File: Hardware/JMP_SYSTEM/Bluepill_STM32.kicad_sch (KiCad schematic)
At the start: 2 parts, among them J1 BLUEPILL

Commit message: Schematics and PCB layout
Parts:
- removed J?: BLUEPILL, Package_DIP:DIP-40_W15.24mm_Socket_LongPads, symbol Connector_Generic:Conn_02x20_Counter_Clockwise
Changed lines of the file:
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@@
-    (pin "9")
-  )
-  (symbol (lib_id "Connector_Generic:Conn_02x20_Counter_Clockwise") (at 160.02 62.865 0) (unit 1)
-    (in_bom yes) (on_board yes)
-    (property "Reference" "J?" (id 0) (at 161.925 24.765 0))
-    (property "Value" "BLUEPILL" (id 1) (at 161.925 27.305 0))
-    (property "Footprint" "Package_DIP:DIP-40_W15.24mm_Socket_LongPads" (id 2) (at 161.925 29.845 0)
-      (effects (font (size 1.27 1.27)) hide)
-    )
-    (property "Datasheet" "~" (id 3) (at 160.02 62.865 0)
-      (effects (font (size 1.27 1.27)) hide)
-    )
-    (pin "1")
-    (pin "10")
-    (pin "11")
-    (pin "12")
-    (pin "13")
-    (pin "14")
-    (pin "15")
-    (pin "16")
-    (pin "17")
-    (pin "18")
-    (pin "19")
-    (pin "2")
-    (pin "20")
-    (pin "21")
-    (pin "22")
-    (pin "23")
-    (pin "24")
-    (pin "25")
-    (pin "26")
-    (pin "27")
-    (pin "28")
-    (pin "29")
-    (pin "3")
-    (pin "30")
-    (pin "31")
-    (pin "32")
-    (pin "33")
-    (pin "34")
-    (pin "35")
-    (pin "36")
-    (pin "37")
-    (pin "38")
-    (pin "39")
-    (pin "4")
-    (pin "40")
-    (pin "5")
-    (pin "6")
-    (pin "7")
-    (pin "8")
     (pin "9")
   )

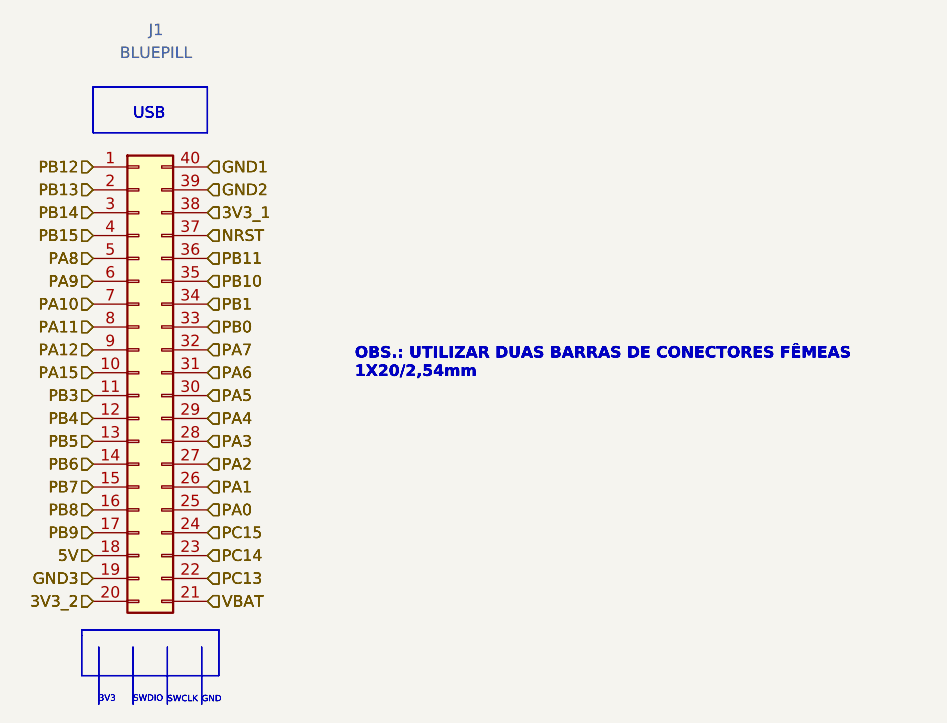
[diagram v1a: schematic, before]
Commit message: Roteamento considerando I2C e Display em conjunto. O display ficara suspenso. Adicionado molex em todos os conectores. Debugs sao pinos convencionais
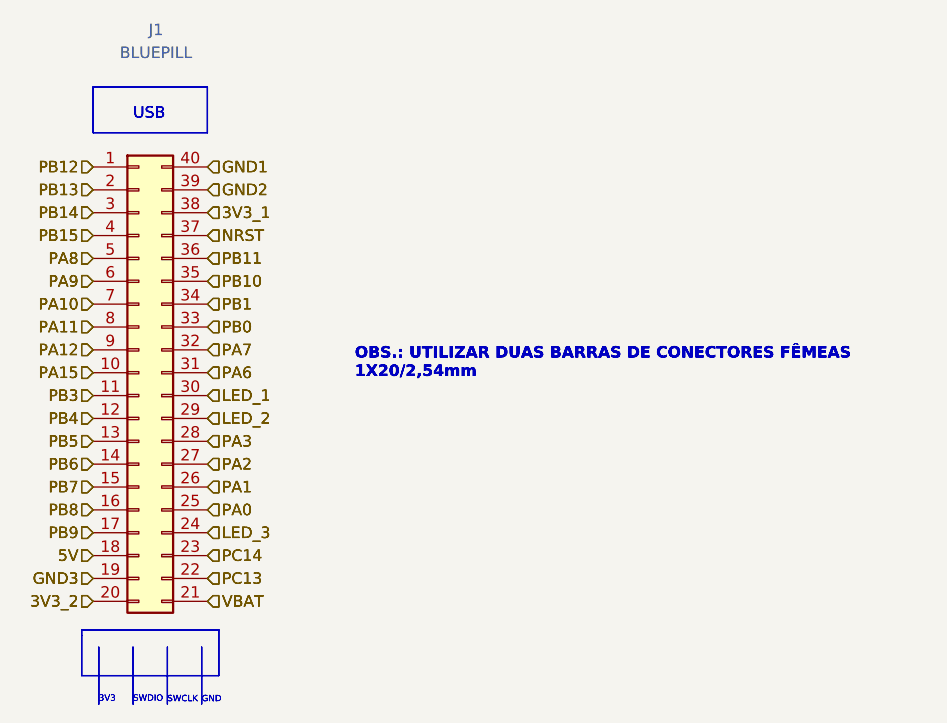
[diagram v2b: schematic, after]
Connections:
- net PA4 renamed LED_2
- net PA5 renamed LED_1
- net PC15 renamed LED_3
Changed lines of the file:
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@@
     (effects (font (size 1.27 1.27)) (justify left))
   )
-  (hierarchical_label "PC15" (shape input) (at 167.64 80.645 0)
+  (hierarchical_label "LED_3" (shape input) (at 167.64 80.645 0)
     (effects (font (size 1.27 1.27)) (justify left))
   )
-  (hierarchical_label "PC15" (shape input) (at 167.64 80.645 0)
+  (hierarchical_label "LED_3" (shape input) (at 167.64 80.645 0)
     (effects (font (size 1.27 1.27)) (justify left))
   )
@@
     (effects (font (size 1.27 1.27)) (justify left))
   )
-  (hierarchical_label "PA5" (shape input) (at 167.64 65.405 0)
+  (hierarchical_label "LED_1" (shape input) (at 167.64 65.405 0)
     (effects (font (size 1.27 1.27)) (justify left))
   )
-  (hierarchical_label "PA5" (shape input) (at 167.64 65.405 0)
+  (hierarchical_label "LED_1" (shape input) (at 167.64 65.405 0)
     (effects (font (size 1.27 1.27)) (justify left))
   )
@@
     (effects (font (size 1.27 1.27)) (justify right))
   )
-  (hierarchical_label "PA4" (shape input) (at 167.64 67.945 0)
+  (hierarchical_label "LED_2" (shape input) (at 167.64 67.945 0)
     (effects (font (size 1.27 1.27)) (justify left))
   )
-  (hierarchical_label "PA4" (shape input) (at 167.64 67.945 0)
+  (hierarchical_label "LED_2" (shape input) (at 167.64 67.945 0)
     (effects (font (size 1.27 1.27)) (justify left))
   )
